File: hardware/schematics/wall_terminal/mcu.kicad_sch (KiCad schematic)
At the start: 1 part, among them U1 ATtiny13A-P

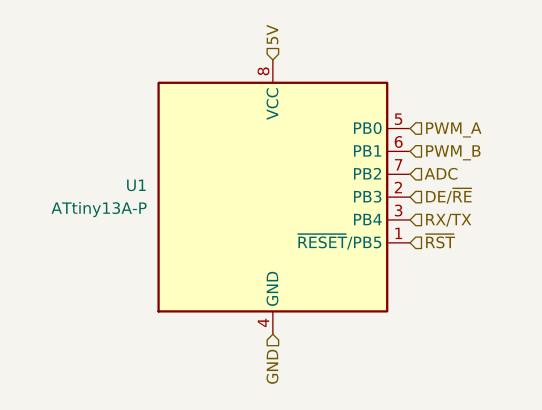
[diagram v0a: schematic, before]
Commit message: fix: added optional resistors on PWM outputs.
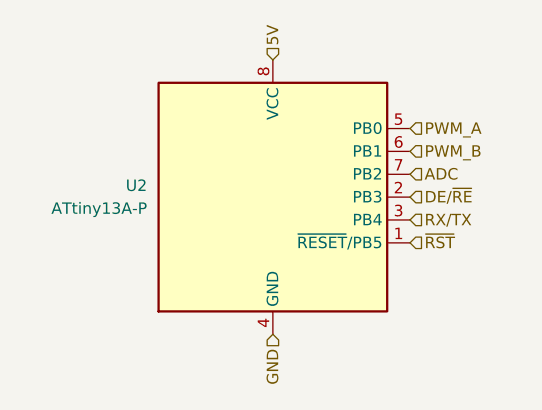
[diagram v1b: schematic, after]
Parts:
- renumbered U1 to U2
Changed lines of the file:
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@@
 		(dnp no)
 		(fields_autoplaced yes)
-		(property "Reference" "U1"
+		(property "Reference" "U2"
 			(at 125.73 87.6299 0)
 			(effects
@@
 			(project "wall_terminal"
 				(path "/5c441dea-07fa-47c6-a7dc-b1c524c62a23/8a2a1432-423c-44a2-bc52-34f5f7caec87"
-					(reference "U1")
+					(reference "U2")
 					(unit 1)
 				)
